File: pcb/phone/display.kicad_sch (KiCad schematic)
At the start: 1 part

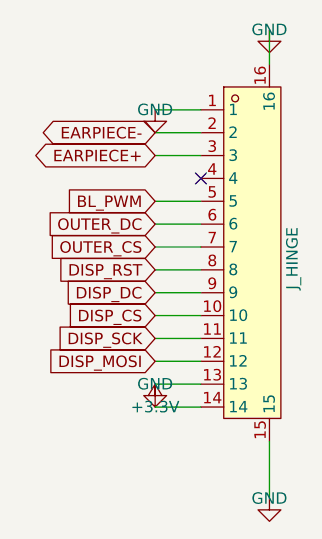
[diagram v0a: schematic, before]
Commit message: Cleanup: remove rejected part symbols, one-off scripts, stale datasheets
- Remove 7 rejected symbols from easyeda2kicad.kicad_sym (PJ-327C-4A,
  PJ-3250-5A, PJ-3240-5A, TYPE-C16PLC-H10.0, PJ-327A5JJ, PJ-327-P5,
  TYPEC-306DDW-ARP16) — replaced by Tensility 54-00298 and GCT USB4085-GF-A
- Delete 10 one-off inspection scripts (check_*.py, find_*.py, dump_*.py,
  extract_*.py) — keep only gen_*.py schematic generators
- Delete rejected datasheets (pj3126-5a, pj3240-5a, pj3250-5a, pj3f07-5p,
  N114 superseded display)
- Delete generated BOM/POS CSV files
- Add alps-ssss2.pdf and gct-usb4085.pdf to reference README index
- Include all schematic changes from previous sessions (SD pullups, VBUS
  divider fix, level shifter verification, codec caps, DCVDD fix)

Generated with [Devin](https://devin.ai)

Co-Authored-By: Devin <158243242+devin-ai-integration[bot]@users.noreply.github.com>
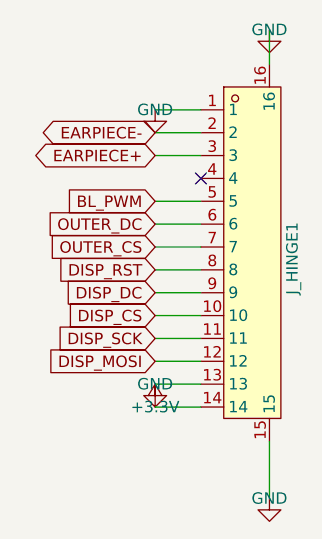
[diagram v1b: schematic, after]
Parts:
- renumbered J_HINGE to J_HINGE1
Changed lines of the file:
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@@
 		(dnp no)
 		(fields_autoplaced yes)
-		(property "Reference" "#PWR130"
+		(property "Reference" "#PWR0125"
 			(at 120.65 113.03 0)
 			(hide yes)
@@
 			(project "phone"
 				(path "/451c3b43-1616-42cb-bf96-d436f4db82c2/d7f57b90-9db7-4266-b1f1-7949b1054009"
-					(reference "#PWR130")
+					(reference "#PWR0125")
 					(unit 1)
 				)
@@
 		(dnp no)
 		(fields_autoplaced yes)
-		(property "Reference" "#PWR132"
+		(property "Reference" "#PWR0128"
 			(at 133.35 156.21 0)
 			(hide yes)
@@
 			(project "phone"
 				(path "/451c3b43-1616-42cb-bf96-d436f4db82c2/d7f57b90-9db7-4266-b1f1-7949b1054009"
-					(reference "#PWR132")
+					(reference "#PWR0128")
 					(unit 1)
 				)
@@
 		(in_pos_files yes)
 		(dnp no)
-		(property "Reference" "J_HINGE"
+		(property "Reference" "J_HINGE1"
 			(at 135.89 129.54 90)
 			(show_name no)
@@
 			(project "phone"
 				(path "/451c3b43-1616-42cb-bf96-d436f4db82c2/d7f57b90-9db7-4266-b1f1-7949b1054009"
-					(reference "J_HINGE")
+					(reference "J_HINGE1")
 					(unit 1)
 				)
@@
 		(dnp no)
 		(fields_autoplaced yes)
-		(property "Reference" "#PWR131"
+		(property "Reference" "#PWR0124"
 			(at 133.35 104.14 0)
 			(hide yes)
@@
 			(project "phone"
 				(path "/451c3b43-1616-42cb-bf96-d436f4db82c2/d7f57b90-9db7-4266-b1f1-7949b1054009"
-					(reference "#PWR131")
+					(reference "#PWR0124")
 					(unit 1)
 				)
@@
 		(dnp no)
 		(fields_autoplaced yes)
-		(property "Reference" "#PWR128"
+		(property "Reference" "#PWR0127"
 			(at 120.65 146.05 0)
 			(hide yes)
@@
 			(project "phone"
 				(path "/451c3b43-1616-42cb-bf96-d436f4db82c2/d7f57b90-9db7-4266-b1f1-7949b1054009"
-					(reference "#PWR128")
+					(reference "#PWR0127")
 					(unit 1)
 				)
@@
 		(dnp no)
 		(fields_autoplaced yes)
-		(property "Reference" "#PWR129"
+		(property "Reference" "#PWR0126"
 			(at 120.65 143.51 0)
 			(hide yes)
@@
 			(project "phone"
 				(path "/451c3b43-1616-42cb-bf96-d436f4db82c2/d7f57b90-9db7-4266-b1f1-7949b1054009"
-					(reference "#PWR129")
-					(unit 1)
-				)
+					(reference "#PWR0126")
+					(unit 1)
+				)

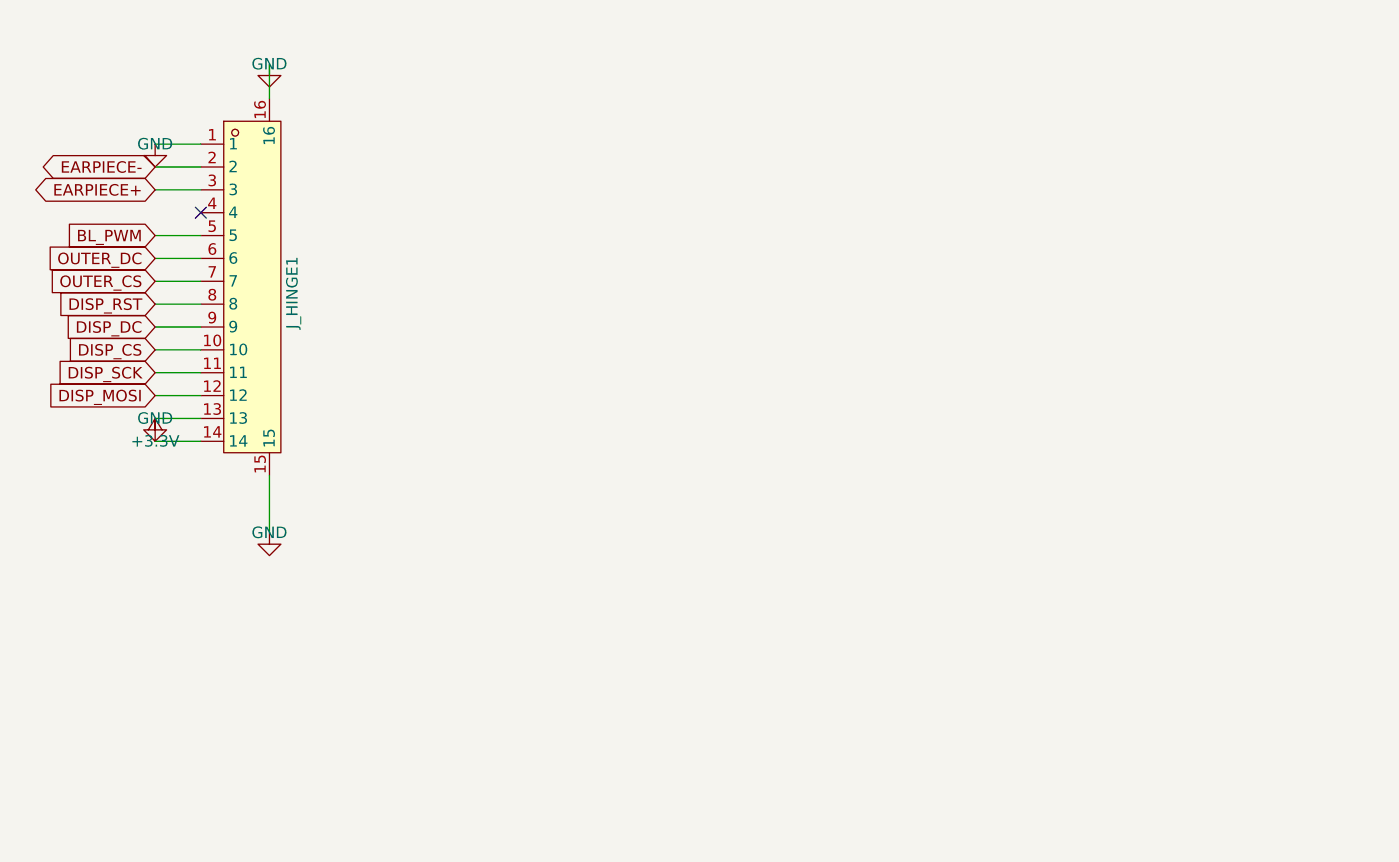
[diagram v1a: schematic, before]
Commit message: Restructure display sheet for candybar + fix pinout + add backlight FET + power switch reversal
Display sheet (LOCKED):
- Fix J_DISP1 pinout to match HS20HS072RX datasheet (was 1/12 correct, now all 14 pins match)
- Add backlight FET circuit: Q1 (AO3400A), R20 (100ohm gate), R5 (10k pulldown), R19 moved to pin 10
- Fix R19 MPN: was 470ohm part with 4.7ohm value, swapped to RC0603JR-074R7L (correct 4.7ohm)
- Move display power from +1V8 to +3.3V (1.8V below VCC min 2.4V)
- Remove display_daughter sheet entry, J_HINGE1, J_HINGE2, OUTER_CS/OUTER_DC
- Add no-connect flags on MCU PG9/PG10 (freed from outer display)
- FPC connector orientation review flagged for PCB layout phase

Power switch (reversed 2026-08-27):
- Move SW21 from battery path back to TPS63021 EN pin (signal-level)
- Select C&K OS102011MA1QN1 (100mA SPDT, LCSC C226259), 8.4mm actuator, usable as finger toggle
- Battery always connected, charging while off restored
- Supersedes 2026-08-17 battery-path architecture

New library parts:
- ics:AO3400A (N-ch MOSFET, SOT-23, LCSC C20917)
- passives:0603WAF1000T5E (100ohm 0603, LCSC C22775)
- passives:RC0603JR-074R7L (4.7ohm 0603, LCSC C137621)
- electromech:OS102011MA1QN1 (SPDT slide switch, LCSC C226259)

Docs updated:
- project-log: 3 new entries (display review, power switch reversal, USB hub)
- bom.md: item 25b switch selected, display backlight parts
- block-diagram.md: +BATT net (no switch), U8 EN pin (switched by SW21)
- schematic-completion-plan.md: display sheet LOCKED, section F complete
- task-tracker.md: O2 updated with 2026-08-27 architecture
- ic-by-ic-review.md: Q3 superseded again, DEF-001 updated
- datasheets/README.md: HS20HS072RX pinout verified, SPI confirmed

Generated with [Devin](https://devin.ai)

Co-Authored-By: Devin <158243242+devin-ai-integration[bot]@users.noreply.github.com>
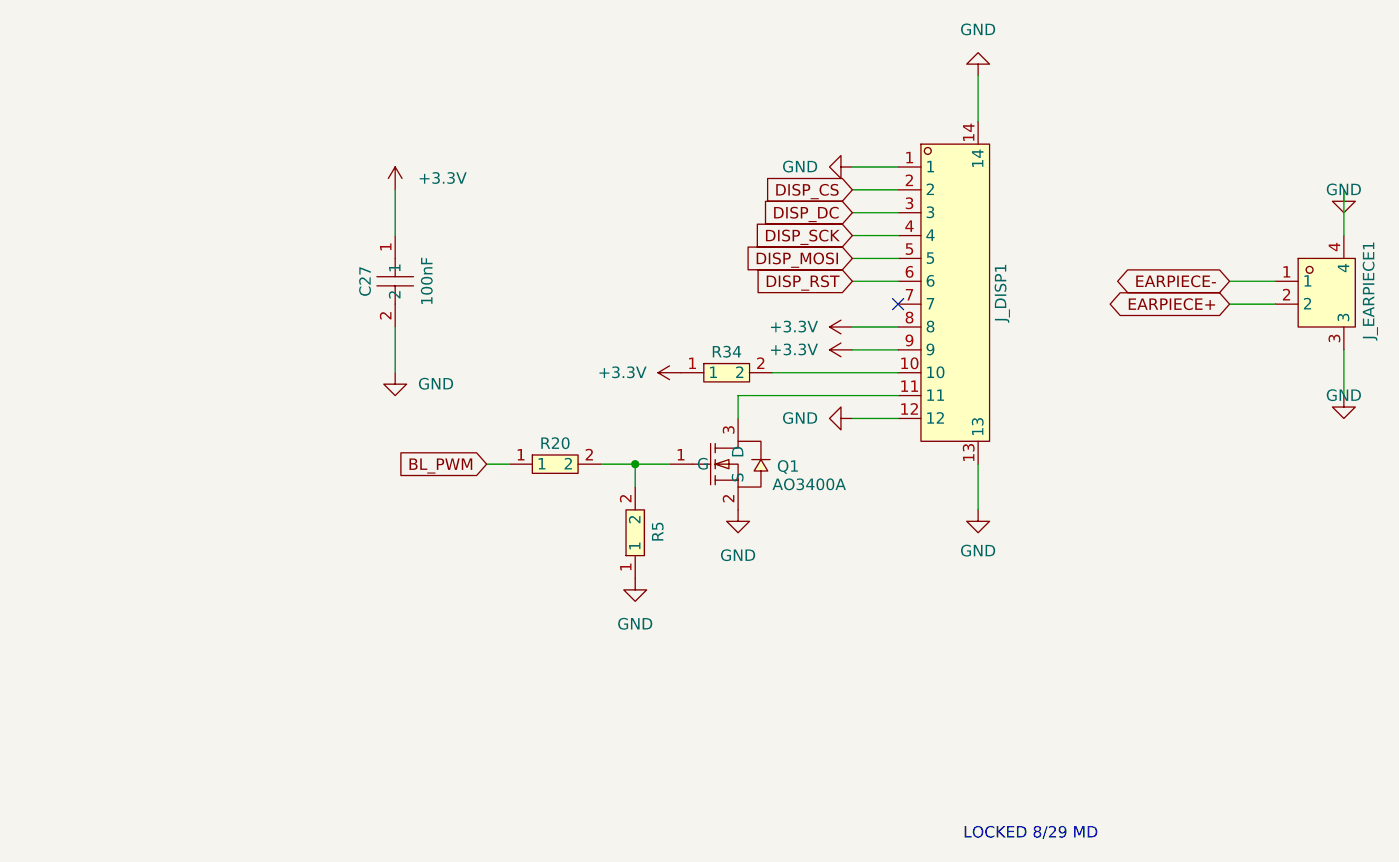
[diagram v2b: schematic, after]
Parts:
- removed J_HINGE1: 0.5K-HX-14PWB, easyeda2kicad:FPC-SMD_14P-P0.50_HDGC_0.5K-HX-14PWB, symbol connectors:0.5K-HX-14PWB
- added C27: 100nF, easyeda2kicad:C0603, symbol passives:CC0603KRX7R9BB104
- added J_DISP1: 0.5K-HX-12PWB, easyeda2kicad:FPC-SMD_12P-P0.50_HDGC_0.5K-HX-12PWB, symbol connectors:0.5K-HX-12PWB
- added J_EARPIECE1: S2B-PH-SM4-TB, easyeda2kicad:CONN-SMD_P2.00_S2B-PH-SM4-TB-LF-SN, symbol connectors:S2B-PH-SM4-TB
- added Q1: AO3400A, easyeda2kicad:SOT-23-3_L2.9-W1.3-P1.90-LS2.4-BR, symbol ics:AO3400A
- added R20: 0603WAF1000T5E, easyeda2kicad:R0603, symbol passives:0603WAF1000T5E
- added R34: RC0603JR-074R7L, easyeda2kicad:R0603, symbol passives:RC0603JR-074R7L
- added R5: RC0603JR-0710KL, easyeda2kicad:R0603, symbol passives:RC0603JR-0710KL
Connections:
- net +3.3V: now also C27.1, J_DISP1.8, J_DISP1.9, R34.1
- net BL_PWM: now also R20.1
- net DISP_CS: now also J_DISP1.2
- net DISP_DC: now also J_DISP1.3
- net DISP_MOSI: now also J_DISP1.5
- net DISP_RST: now also J_DISP1.6
- net DISP_SCK: now also J_DISP1.4
- net EARPIECE+: now also J_EARPIECE1.2
- net EARPIECE-: now also J_EARPIECE1.1
- net GND: now also C27.2, J_DISP1.1, J_DISP1.12, J_DISP1.13, J_DISP1.14, J_EARPIECE1.3, J_EARPIECE1.4, Q1.2 (S), R5.1
- new net: J_DISP1.10, R34.2
- new net: J_DISP1.11, Q1.3 (D)
- new net: Q1.1 (G), R20.2, R5.2
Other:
- note added: "LOCKED 8/29 MD"
